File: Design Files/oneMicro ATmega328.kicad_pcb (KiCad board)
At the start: 2 copper layers, 18 x 35.3 mm, 28 parts, among them CON1 USB-MINI-B, IC1 ATMEGA328-P, IC2 MIC5205, P14 CONN_01X01, P2 CONN_01X12, P3 CONN_01X02, P5 CONN_01X12, SW1 RESET, U1 CP2102, X1 16MHz

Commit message: Design Completed
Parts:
- added P1: CONN_01X02, Pin_Headers:Pin_Header_Straight_1x02, F.Cu at (165.5, 116.2)
- C1, C2, C3, C4, C6, C7, C8, C9, F1, IC2, R3: moved to F.Cu
- D4: footprint EE:ZenerDiode_SMD_new -> Diodes_SMD:SOD-123; moved to F.Cu
- IC1: value ATMEGA328-P -> ATMEGA328P-A
- moved IC2 25.7 mm to (157.1, 118.6)
- moved C7 25.4 mm to (155.6, 122.7), turned to 270 degrees
- moved C3 17.8 mm to (163.0, 119.1)
- moved C8 17.4 mm to (160.3, 117.8), turned to 90 degrees
- moved R3 15.9 mm to (165.8, 124.1), turned to 180 degrees
- moved C6 15.2 mm to (168.1, 92.1), turned to 180 degrees
- moved C9 14.4 mm to (157.3, 116.2)
- moved C1 14.4 mm to (165.1, 96.0)
- moved P3 13.4 mm to (165.5, 105.7), turned to 180 degrees
- moved R2 13.1 mm to (165.4, 109.3), turned to 270 degrees
- moved C2 11.3 mm to (165.3, 121.6), turned to 270 degrees
- moved X1 10.1 mm to (156.8, 106.5), turned to 45 degrees
- moved C4 10.1 mm to (165.3, 100.5), turned to 270 degrees
- moved R8 9.19 mm to (155.2, 92.7)
- moved D3 7.07 mm to (153.1, 92.7), turned to 180 degrees
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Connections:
- D1 pad 1: /SCK -> Net-(D1-Pad1)
- D1 pad 2: Net-(D1-Pad2) -> /SCK
- IC1 pad 1: /RESET -> /D3
- IC1 pad 10: Net-(IC1-Pad10) -> /D6
- IC1 pad 11: /D5 -> /D7
- IC1 pad 12: /D6 -> /D8
- IC1 pad 13: /D7 -> /D9
- IC1 pad 14: /D8 -> /D10
- IC1 pad 15: /D9 -> /MOSI
- IC1 pad 16: /D10 -> /MISO
- IC1 pad 17: /MOSI -> /SCK
- IC1 pad 18: /MISO -> VCC
- IC1 pad 19: /SCK -> /A6
- IC1 pad 2: /RXD -> /D4
- IC1 pad 20: VCC -> Net-(C2-Pad1)
- IC1 pad 21: Net-(C2-Pad1) -> GND
- IC1 pad 22: GND -> /A7
- IC1 pad 29: (no net) -> /RESET
- IC1 pad 3: /TXD -> GND
- IC1 pad 30: (no net) -> /RXD
- IC1 pad 31: (no net) -> /TXD
- IC1 pad 32: (no net) -> /D2
- IC1 pad 4: /D2 -> VCC
- IC1 pad 5: /D3 -> GND
- IC1 pad 6: /D4 -> Net-(IC1-Pad6)
- IC1 pad 7: VCC -> Net-(IC1-Pad7)
- IC1 pad 9: Net-(IC1-Pad9) -> /D5
- P2 pad 10: GND -> /RESET
- P2 pad 11: /RXD1 -> /RXD
- P2 pad 12: /TXD0 -> /TXD
- R4 pad 1: VCC -> GND
- R4 pad 2: Net-(D1-Pad2) -> Net-(D1-Pad1)
- X1 pad 1: Net-(IC1-Pad10) -> Net-(IC1-Pad8)
- X1 pad 2: Net-(IC1-Pad9) -> Net-(IC1-Pad7)
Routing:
- net GND: track 0.00 -> 103.1 mm, vias 0 -> 13
- net VCC: track 0.00 -> 90.5 mm, vias 0 -> 10
- net /RESET: track 0.00 -> 63.5 mm, vias 0 -> 5
- net /RAW: track 0.00 -> 42.4 mm, vias 0 -> 5
- net /RXD: track 0.00 -> 22.5 mm
- net /TXD: track 0.00 -> 19.7 mm, vias 0 -> 1
- net /D10: track 0.00 -> 16.9 mm
- net Net-(D4-Pad1): track 0.00 -> 14.4 mm, vias 0 -> 2
- net Net-(C6-Pad2): track 0.00 -> 13.9 mm, vias 0 -> 2
- net /MOSI: track 0.00 -> 13.7 mm
- net /D9: track 0.00 -> 12.3 mm
- net Net-(CON1-Pad3): track 0.00 -> 11.2 mm, vias 0 -> 2
- net Net-(C2-Pad1): track 0.00 -> 10.4 mm, vias 0 -> 2
- net /D8: track 0.00 -> 10.1 mm
- net /D4: track 0.00 -> 10.1 mm
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- added copper zone on B.Cu, net GND
- added copper zone on F.Cu, net VCC
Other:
- board size 18 x 35.3 mm -> 18 x 35.2 mm
- net class Default: clearance 0.1651 -> 0.1
- rule trace_clearance: 0.1651 -> 0.1
- rule trace_min: 0.254 -> 0.13
- rule via_min_size: 0.6 -> 0.5
- board text added: "11"
- board text added: "12"
- board text added: "13"
- board text added: "ATmega328"
- board text added: "ExploreEmbedded"
- board text added: "oneMicro"
- board text removed: "MISO"
- board text removed: "MOSI"
- board text removed: "SCK"
- board text removed: "SCL"
- board text removed: "SDA"

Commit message: changes in silk and layout
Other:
- outline, holes or cut-outs redrawn
- board text added: "328"
- board text added: "RXI"
- board text added: "TXO"
- board text removed: "ATmega328"
- board text removed: "RX1"
- board text removed: "TX0"

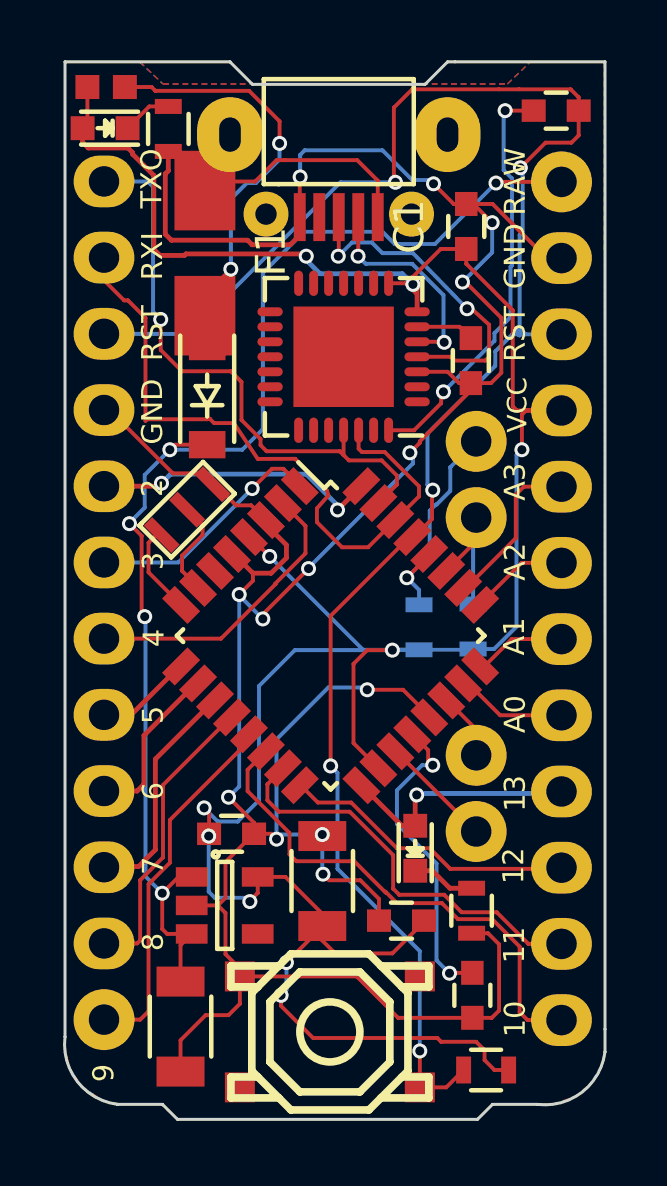
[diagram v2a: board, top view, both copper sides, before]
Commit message: Board outline modified
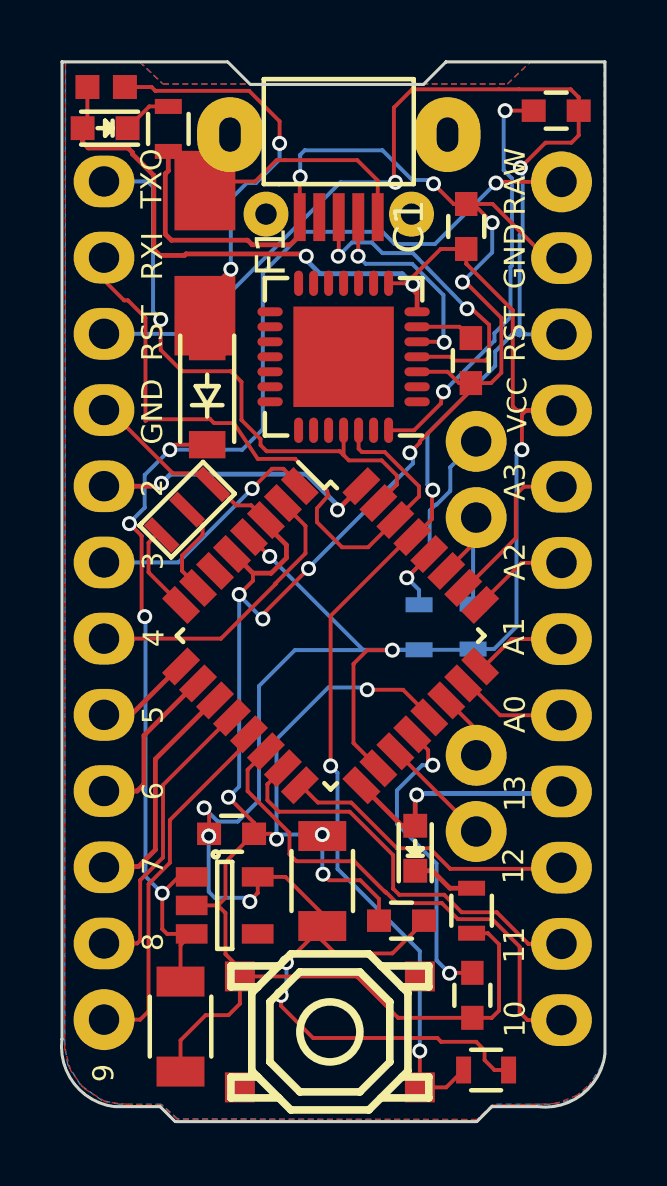
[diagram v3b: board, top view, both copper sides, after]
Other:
- board size 18 x 35.2 mm -> 18.1 x 35.3 mm
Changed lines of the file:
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@@
-(kicad_pcb (version 4) (host pcbnew "(2015-01-16 BZR 5376)-product")
+(kicad_pcb (version 4) (host pcbnew 4.0.1-stable)
   (general
     (links 80)
     (no_connects 0)
-    (area 151.684435 90.449999 169.800001 125.800001)
+    (area 151.582835 90.437499 169.800001 125.876201)
     (thickness 1.6)
-    (drawings 70)
+    (drawings 68)
     (tracks 602)
     (zones 0)
@@
       (net 2 GND))
   )
-  (module EE:Pin_Header_Straight_1x20_New locked (layer B.Cu)
+  (module EE:Pin_Header_Straight_1x20_New (layer B.Cu)
     (at 153.05 122.425)
     (descr "Through hole pin header")
@@
       (net 53 "Net-(D4-Pad1)"))
   )
-  (gr_line (start 163.75 91.25) (end 158 91.25) (angle 90) (layer Edge.Cuts) (width 0.1))
-  (gr_line (start 164.5 90.5) (end 163.75 91.25) (angle 90) (layer Edge.Cuts) (width 0.1))
-  (gr_line (start 164.75 90.5) (end 164.5 90.5) (angle 90) (layer Edge.Cuts) (width 0.1))
-  (gr_line (start 164.75 90.5) (end 169.75 90.5) (angle 90) (layer Edge.Cuts) (width 0.1))
-  (gr_line (start 157.25 90.5) (end 158 91.25) (angle 90) (layer Edge.Cuts) (width 0.1))
-  (gr_line (start 151.75 90.5) (end 157.25 90.5) (angle 90) (layer Edge.Cuts) (width 0.1))
+  (gr_line (start 169.7482 123.5456) (end 169.7482 90.5002) (angle 90) (layer Edge.Cuts) (width 0.1))
+  (gr_arc (start 153.6484 123.3262) (end 153.3984 125.3262) (angle 90) (layer Edge.Cuts) (width 0.1))
+  (gr_line (start 154.9238 125.3262) (end 153.4238 125.3262) (angle 90) (layer Edge.Cuts) (width 0.1))
+  (gr_line (start 155.4238 125.8262) (end 154.9238 125.3262) (angle 90) (layer Edge.Cuts) (width 0.1))
+  (gr_line (start 165.4492 125.8262) (end 155.4492 125.8262) (angle 90) (layer Edge.Cuts) (width 0.1))
+  (gr_line (start 165.9746 125.3262) (end 165.4746 125.8262) (angle 90) (layer Edge.Cuts) (width 0.1))
+  (gr_line (start 167.4746 125.3262) (end 165.9746 125.3262) (angle 90) (layer Edge.Cuts) (width 0.1))
+  (gr_line (start 151.6507 90.4875) (end 151.6507 123.0757) (angle 90) (layer Edge.Cuts) (width 0.1))
+  (gr_line (start 151.6484 90.5) (end 157.1484 90.5) (angle 90) (layer Edge.Cuts) (width 0.1))
+  (gr_line (start 157.1738 90.5) (end 157.9238 91.25) (angle 90) (layer Edge.Cuts) (width 0.1))
+  (gr_line (start 164.4492 90.5) (end 163.6992 91.25) (angle 90) (layer Edge.Cuts) (width 0.1))
+  (gr_line (start 164.4396 90.5002) (end 169.7482 90.5002) (angle 90) (layer Edge.Cuts) (width 0.1))
+  (gr_line (start 163.6992 91.25) (end 157.9492 91.25) (angle 90) (layer Edge.Cuts) (width 0.1))
   (gr_text ExploreEmbedded (at 162.5854 117.8052 90) (layer B.SilkS)
     (effects (font (size 1 1) (thickness 0.25)) (justify mirror))
@@
     (effects (font (size 1 1) (thickness 0.25)) (justify mirror))
   )
-  (gr_line (start 151.75 123) (end 151.75 90.5) (angle 90) (layer Edge.Cuts) (width 0.1))
-  (gr_line (start 155 125.25) (end 153.5 125.25) (angle 90) (layer Edge.Cuts) (width 0.1))
-  (gr_arc (start 153.75 123.25) (end 153.5 125.25) (angle 90) (layer Edge.Cuts) (width 0.1))
-  (gr_line (start 155.5 125.75) (end 155 125.25) (angle 90) (layer Edge.Cuts) (width 0.1))
-  (gr_line (start 165.5 125.75) (end 155.5 125.75) (angle 90) (layer Edge.Cuts) (width 0.1))
-  (gr_line (start 169.75 122.75) (end 169.75 123.5) (angle 90) (layer Edge.Cuts) (width 0.1))
-  (gr_line (start 166 125.25) (end 165.5 125.75) (angle 90) (layer Edge.Cuts) (width 0.1))
-  (gr_line (start 167.5 125.25) (end 166 125.25) (angle 90) (layer Edge.Cuts) (width 0.1))
-  (gr_arc (start 167.75 123.25) (end 169.75 123.5) (angle 90) (layer Edge.Cuts) (width 0.1))
-  (gr_line (start 169.75 90.5) (end 169.75 122.75) (angle 90) (layer Edge.Cuts) (width 0.1))
+  (gr_arc (start 167.75 123.3262) (end 169.75 123.5762) (angle 90) (layer Edge.Cuts) (width 0.1))
   (gr_text 3.3V (at 158.0134 110.9726 90) (layer B.SilkS)
     (effects (font (size 0.8 0.8) (thickness 0.2)) (justify mirror))

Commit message: Gerber file generated
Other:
- board text added: "v0.1"
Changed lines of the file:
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@@
     (area 151.582835 90.437499 169.800001 125.876201)
     (thickness 1.6)
-    (drawings 68)
+    (drawings 71)
     (tracks 602)
     (zones 0)
@@
   (page A3)
   (layers
-    (0 F.Cu signal)
-    (31 B.Cu signal)
+    (0 F.Cu signal hide)
+    (31 B.Cu signal hide)
     (32 B.Adhes user)
     (33 F.Adhes user)
@@
     (visible_elements 7FFEFF7F)
     (pcbplotparams
-      (layerselection 0x00010_00000000)
+      (layerselection 0x000f0_80000001)
       (usegerberextensions true)
-      (excludeedgelayer true)
+      (excludeedgelayer false)
       (linewidth 0.150000)
       (plotframeref false)
@@
       (drillshape 0)
       (scaleselection 1)
-      (outputdirectory ""))
+      (outputdirectory "Gerber Files/"))
   )
   (net 0 "")
@@
       (net 53 "Net-(D4-Pad1)"))
   )
+  (gr_text v0.1 (at 160.8328 92.8624) (layer B.SilkS)
+    (effects (font (size 1 1) (thickness 0.25)) (justify mirror))
+  )
+  (dimension 35.307791 (width 0.3) (layer B.CrtYd)
+    (gr_text "35.308 mm" (at 175.25384 108.071981 270.5770603) (layer B.CrtYd)
+      (effects (font (size 1.5 1.5) (thickness 0.3)))
+    )
+    (feature1 (pts (xy 164.4904 90.5256) (xy 176.425972 90.405385)))
+    (feature2 (pts (xy 164.846 125.8316) (xy 176.781572 125.711385)))
+    (crossbar (pts (xy 174.081709 125.738578) (xy 173.726109 90.432578)))
+    (arrow1a (pts (xy 173.726109 90.432578) (xy 174.323846 91.553119)))
+    (arrow1b (pts (xy 173.726109 90.432578) (xy 173.151064 91.564931)))
+    (arrow2a (pts (xy 174.081709 125.738578) (xy 174.656754 124.606225)))
+    (arrow2b (pts (xy 174.081709 125.738578) (xy 173.483972 124.618037)))
+  )
+  (dimension 18.084818 (width 0.3) (layer B.CrtYd)
+    (gr_text "18.085 mm" (at 160.671369 129.252151 359.9195285) (layer B.CrtYd)
+      (effects (font (size 1.5 1.5) (thickness 0.3)))
+    )
+    (feature1 (pts (xy 169.7228 122.8344) (xy 169.711873 130.61485)))
+    (feature2 (pts (xy 151.638 122.809) (xy 151.627073 130.58945)))
+    (crossbar (pts (xy 151.630865 127.889453) (xy 169.715665 127.914853)))
+    (arrow1a (pts (xy 169.715665 127.914853) (xy 168.588339 128.499691)))
+    (arrow1b (pts (xy 169.715665 127.914853) (xy 168.589986 127.326851)))
+    (arrow2a (pts (xy 151.630865 127.889453) (xy 152.756544 128.477455)))
+    (arrow2b (pts (xy 151.630865 127.889453) (xy 152.758191 127.304615)))
+  )
   (gr_line (start 169.7482 123.5456) (end 169.7482 90.5002) (angle 90) (layer Edge.Cuts) (width 0.1))

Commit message: Exception data cleared
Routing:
- net /D9: track 12.3 -> 13.0 mm, vias 0 -> 1
- net /D6: track 5.57 -> 4.95 mm
- net /D7: track 7.77 -> 7.16 mm
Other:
- net class Default: clearance 0.1 -> 0.13
- rule trace_clearance: 0.1 -> 0.13

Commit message: Changes Done
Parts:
- removed F1: 0.5A, Fuse_Holders_and_Fuses:Fuse_SMD1206_HandSoldering
- D4: footprint Diodes_SMD:SOD-123 -> Explore:Diode_New
- moved R8 3.60 mm to (156.1, 96.2)
- moved D4 0.60 mm to (156.2, 101.1)
- moved JP1 0.20 mm to (153.5, 91.3)
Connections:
- D4 pad 1: Net-(D4-Pad1) -> /VBUS
- JP1 pad 1: Net-(D4-Pad1) -> /VBUS
- X1 pad 2: Net-(IC1-Pad7) -> GND
- X1 pad 3: GND -> Net-(IC1-Pad7)
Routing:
- net Net-(D4-Pad1): track 14.4 -> 0.00 mm, vias 2 -> 0
- net /VBUS: track 7.89 -> 21.4 mm, vias 0 -> 2
- net Net-(IC1-Pad7): track 3.33 -> 5.46 mm
- net Net-(D3-Pad1): track 1.66 -> 3.70 mm
- net VCC: track 90.5 -> 91.9 mm
- net /D2: track 9.80 -> 10.7 mm
- net /RXD: track 22.5 -> 21.9 mm
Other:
- board size 18.1 x 35.3 mm -> 18.1 x 35.4 mm
- board text added: "A6"
- board text added: "A7"
- board text added: "SCL"
- board text added: "SDA"
